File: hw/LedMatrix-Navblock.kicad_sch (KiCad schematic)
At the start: 38 parts, among them Q4200 DTA114E, Q4201 DTA114E, Q4202 DTA114E, Q4203 DTA114E, Q4204 DTA114E, Q4205 DTC114EE, Q4206 DTC114EE, Q4207 DTC114EE, Q4208 DTC114EE, Q4209 DTC114EE, Q4210 DTC114EE, Q4211 DTC114EE, Q4212 DTC114EE, Q4213 DTC114EE

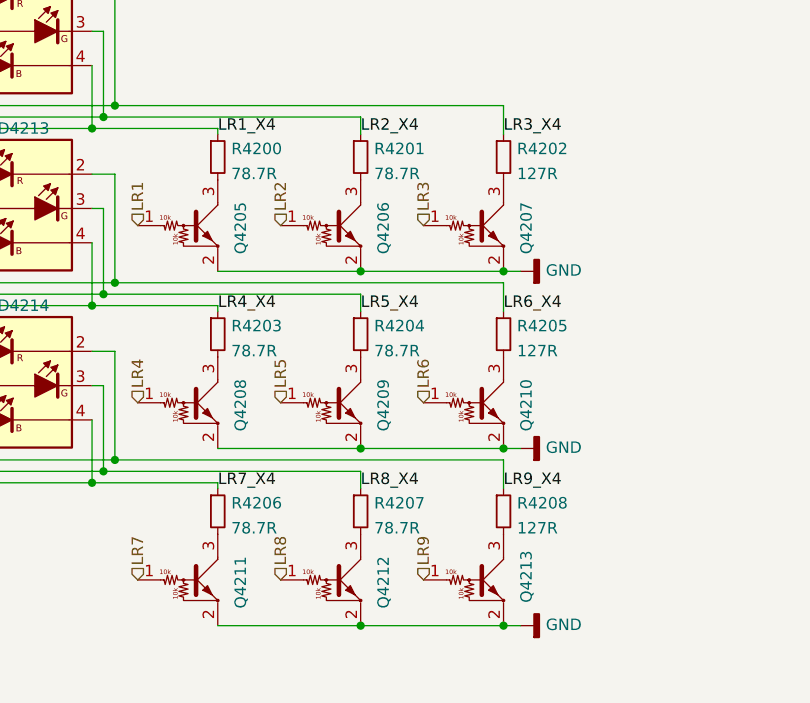
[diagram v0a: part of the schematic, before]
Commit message: Add 300R symbol and use it at green LEDs.
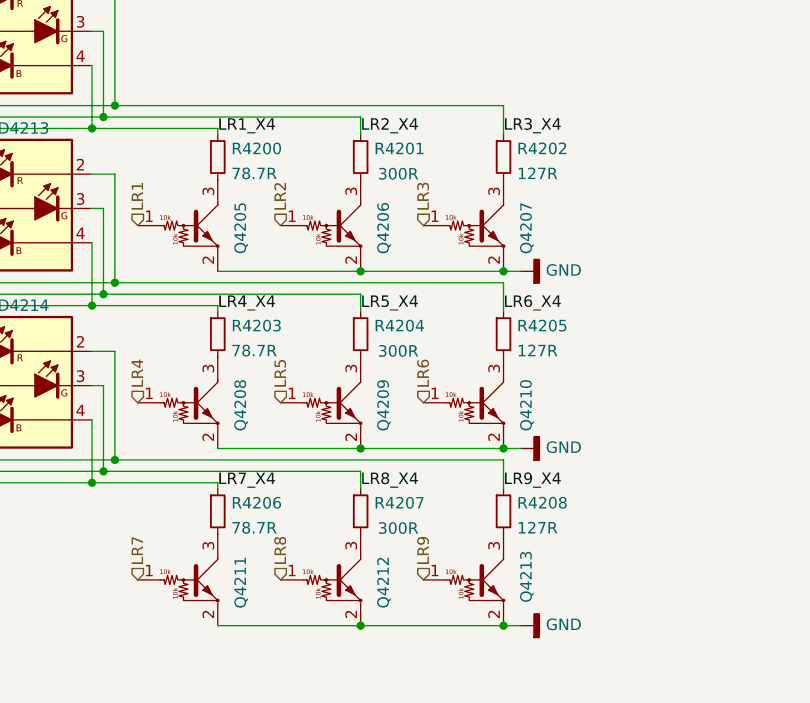
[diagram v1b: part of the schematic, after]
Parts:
- R4201, R4204, R4207: value 78.7R -> 300R; symbol Keyboard:78.7R -> Keyboard:300R; manf# RC0402FR-0778R7L -> ERJ-2RKF3000X; mouser# 603-RC0402FR-0778R7L -> 667-ERJ-2RKF3000X
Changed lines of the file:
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@@
     (pin "3")
   )
-  (symbol (lib_id "Keyboard:78.7R") (at 149.86 97.79 0) (unit 1)
-    (in_bom yes) (on_board yes) (fields_autoplaced)
+  (symbol (lib_id "Keyboard:300R") (at 149.86 97.79 0) (unit 1)
+    (in_bom yes) (on_board yes)
     (property "Reference" "R4207" (id 0) (at 151.3586 96.8815 0)
       (effects (font (size 1.27 1.27)) (justify left))
     )
-    (property "Value" "78.7R" (id 1) (at 151.3586 99.6566 0)
+    (property "Value" "300R" (id 1) (at 151.765 99.695 0)
       (effects (font (size 1.27 1.27)) (justify left))
     )
@@
       (effects (font (size 1.27 1.27)) hide)
     )
-    (property "Datasheet" "https://www.mouser.de/datasheet/2/447/PYu_RC_Group_51_RoHS_L_10-1664068.pdf" (id 3) (at 150.622 97.282 0)
+    (property "Datasheet" "https://www.mouser.de/datasheet/2/315/AOA0000C304-1149620.pdf" (id 3) (at 150.622 97.282 0)
       (effects (font (size 1.27 1.27)) hide)
     )
-    (property "mouser#" "603-RC0402FR-0778R7L" (id 4) (at 153.162 94.742 0)
+    (property "mouser#" "667-ERJ-2RKF3000X" (id 4) (at 153.162 94.742 0)
       (effects (font (size 1.524 1.524)) hide)
     )
-    (property "manf#" "RC0402FR-0778R7L" (id 5) (at 149.86 97.79 0)
+    (property "manf#" "ERJ-2RKF3000X " (id 5) (at 149.86 97.79 0)
       (effects (font (size 1.27 1.27)) hide)
     )
@@
     (pin "2")
   )
-  (symbol (lib_id "Keyboard:78.7R") (at 149.86 78.105 0) (unit 1)
-    (in_bom yes) (on_board yes) (fields_autoplaced)
+  (symbol (lib_id "Keyboard:300R") (at 149.86 78.105 0) (unit 1)
+    (in_bom yes) (on_board yes)
     (property "Reference" "R4204" (id 0) (at 151.3586 77.1965 0)
       (effects (font (size 1.27 1.27)) (justify left))
     )
-    (property "Value" "78.7R" (id 1) (at 151.3586 79.9716 0)
+    (property "Value" "300R" (id 1) (at 151.765 80.01 0)
       (effects (font (size 1.27 1.27)) (justify left))
     )
@@
       (effects (font (size 1.27 1.27)) hide)
     )
-    (property "Datasheet" "https://www.mouser.de/datasheet/2/447/PYu_RC_Group_51_RoHS_L_10-1664068.pdf" (id 3) (at 150.622 77.597 0)
+    (property "Datasheet" "https://www.mouser.de/datasheet/2/315/AOA0000C304-1149620.pdf" (id 3) (at 150.622 77.597 0)
       (effects (font (size 1.27 1.27)) hide)
     )
-    (property "mouser#" "603-RC0402FR-0778R7L" (id 4) (at 153.162 75.057 0)
+    (property "mouser#" "667-ERJ-2RKF3000X" (id 4) (at 153.162 75.057 0)
       (effects (font (size 1.524 1.524)) hide)
     )
-    (property "manf#" "RC0402FR-0778R7L" (id 5) (at 149.86 78.105 0)
+    (property "manf#" "ERJ-2RKF3000X " (id 5) (at 149.86 78.105 0)
       (effects (font (size 1.27 1.27)) hide)
     )
@@
     (pin "2")
   )
-  (symbol (lib_id "Keyboard:78.7R") (at 149.86 58.42 0) (unit 1)
-    (in_bom yes) (on_board yes) (fields_autoplaced)
+  (symbol (lib_id "Keyboard:300R") (at 149.86 58.42 0) (unit 1)
+    (in_bom yes) (on_board yes)
     (property "Reference" "R4201" (id 0) (at 151.3586 57.5115 0)
       (effects (font (size 1.27 1.27)) (justify left))
     )
-    (property "Value" "78.7R" (id 1) (at 151.3586 60.2866 0)
+    (property "Value" "300R" (id 1) (at 151.765 60.325 0)
       (effects (font (size 1.27 1.27)) (justify left))
     )
@@
       (effects (font (size 1.27 1.27)) hide)
     )
-    (property "Datasheet" "https://www.mouser.de/datasheet/2/447/PYu_RC_Group_51_RoHS_L_10-1664068.pdf" (id 3) (at 150.622 57.912 0)
+    (property "Datasheet" "https://www.mouser.de/datasheet/2/315/AOA0000C304-1149620.pdf" (id 3) (at 150.622 57.912 0)
       (effects (font (size 1.27 1.27)) hide)
     )
-    (property "mouser#" "603-RC0402FR-0778R7L" (id 4) (at 153.162 55.372 0)
+    (property "mouser#" "667-ERJ-2RKF3000X" (id 4) (at 153.162 55.372 0)
       (effects (font (size 1.524 1.524)) hide)
     )
-    (property "manf#" "RC0402FR-0778R7L" (id 5) (at 149.86 58.42 0)
+    (property "manf#" "ERJ-2RKF3000X " (id 5) (at 149.86 58.42 0)
       (effects (font (size 1.27 1.27)) hide)
     )
